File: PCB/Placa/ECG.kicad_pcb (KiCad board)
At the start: 2 copper layers, 118.6 x 62.2 mm, 44 parts, among them P1 USB_OTG, P2 CONN_01X03, P3 CONN_01X03, P7 Shield, U1 INA333, U2 OPA2335, U3 OPA2335, U4 REF5050, U5 REF3112, U6 INA333, U7 OPA2335, U8 OPA2335

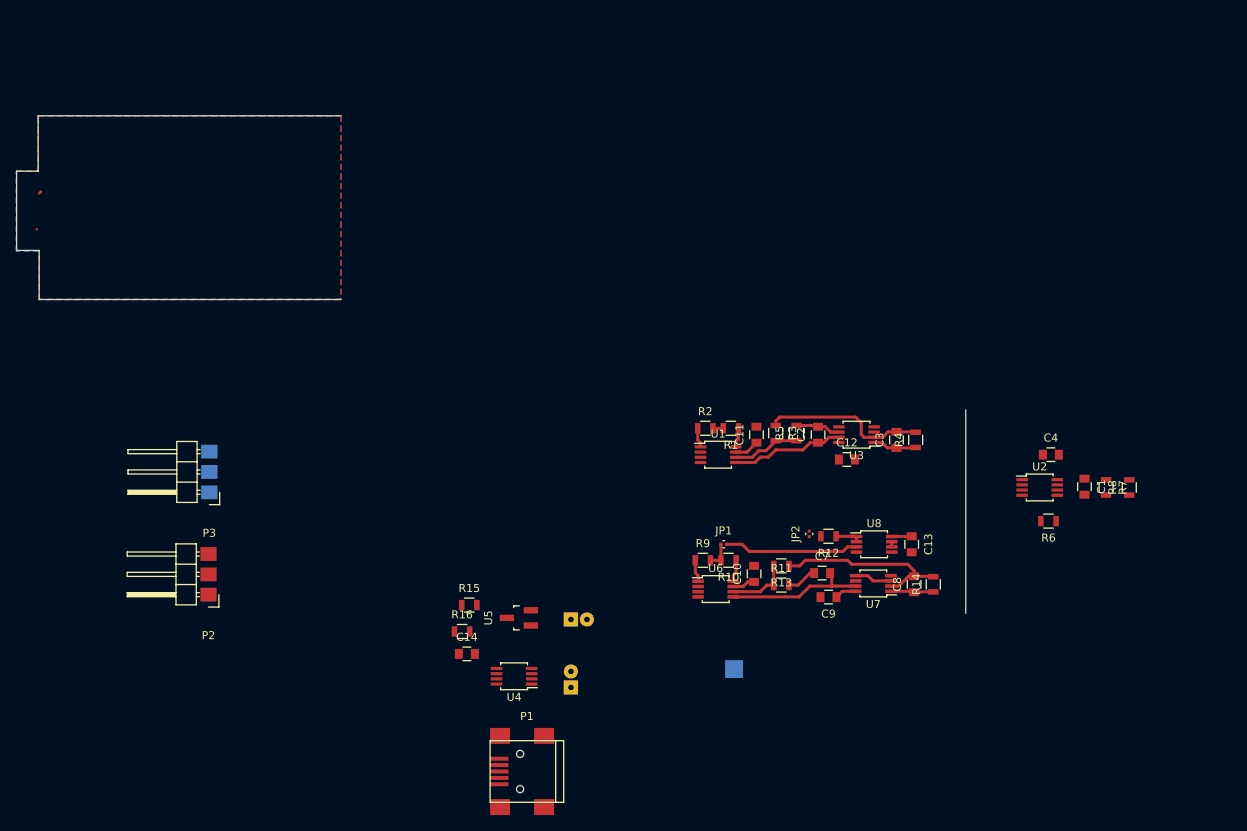
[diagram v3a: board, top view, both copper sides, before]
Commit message: Sigo con la placa. Agregué el micrófono electret
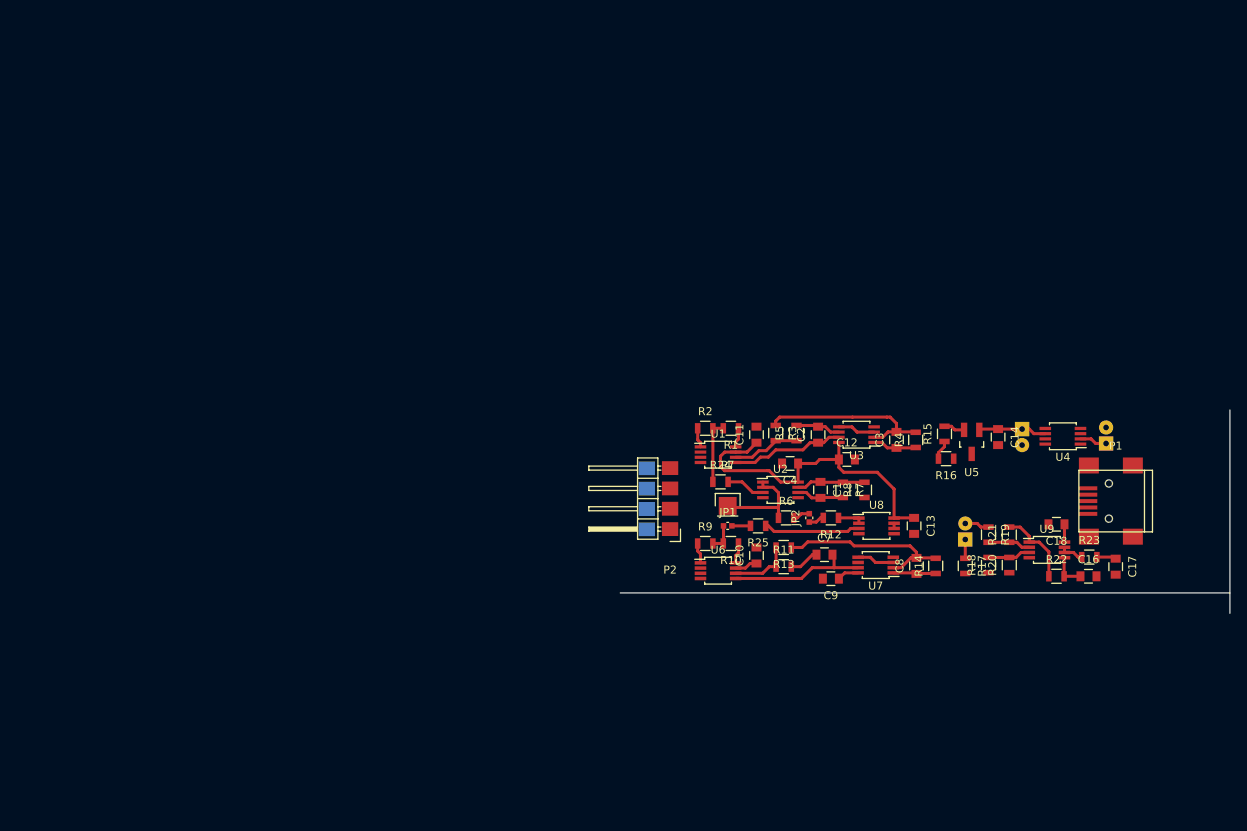
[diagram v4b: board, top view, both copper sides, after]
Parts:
- added C15: 4.7u, Capacitors_ThroughHole:C_Radial_D5_L11_P2, B.Cu at (175.2, 87.3)
- added C16: 470n, Capacitors_SMD:C_0805, F.Cu at (190.6, 91.9)
- added C17: 470n, Capacitors_SMD:C_0805, F.Cu at (194.0, 90.7)
- added C18: 0.1u, Capacitors_SMD:C_0805, F.Cu at (186.6, 85.4)
- added R17: 2.2k, Resistors_SMD:R_0805, F.Cu at (175.2, 90.6)
- added R18: 1.1k, Resistors_SMD:R_0805, F.Cu at (178.1, 90.5)
- added R19: 10k, Resistors_SMD:R_0805, F.Cu at (178.1, 86.7)
- added R20: 2.2k, Resistors_SMD:R_0805, F.Cu at (180.7, 90.5)
- added R21: 100k, Resistors_SMD:R_0805, F.Cu at (180.7, 86.7)
- added R22: 3.3k, Resistors_SMD:R_0805, F.Cu at (186.6, 91.9)
- added R23: 3.3k, Resistors_SMD:R_0805, F.Cu at (190.7, 89.5)
- added R24: 100k, Resistors_SMD:R_0805, F.Cu at (144.6, 80.1)
- added R25: 100k, Resistors_SMD:R_0805, F.Cu at (149.3, 85.6)
- added U9: OPA2335, Housings_SSOP:MSOP-8_3x3mm_Pitch0.65mm, F.Cu at (185.4, 88.6)
- P2: value CONN_01X03 -> CONN_01X04; footprint Pin_Headers:Pin_Header_Angled_1x03 -> Pin_Headers:Pin_Header_Angled_1x04
- P3: value CONN_01X03 -> CONN_01X04; footprint Pin_Headers:Pin_Header_Angled_1x03 -> Pin_Headers:Pin_Header_Angled_1x04; moved to B.Cu
- P7: moved to F.Cu
- moved P1 81.0 mm to (194.0, 82.5)
- moved U4 74.9 mm to (187.4, 74.4)
- moved C5 73.5 mm to (192.8, 75.3)
- moved C14 71.7 mm to (179.3, 74.5), turned to 270 degrees
- moved R16 64.2 mm to (172.8, 77.2), turned to 180 degrees
- moved R15 63.1 mm to (172.6, 74.1), turned to 90 degrees
- moved C6 61.2 mm to (182.3, 73.5), turned to 270 degrees
- moved U5 60.7 mm to (176.0, 75.1), turned to 180 degrees
- moved P2 58.3 mm to (138.3, 86.0)
- moved P3 54.8 mm to (135.4, 78.4)
- moved R8 33.1 mm to (162.6, 81.1)
- moved C1 33.0 mm to (157.1, 81.1)
- moved R7 32.9 mm to (159.9, 81.1)
- moved R6 32.8 mm to (152.8, 84.6), turned to 0 degrees
- moved C4 32.6 mm to (153.3, 77.8), turned to 180 degrees
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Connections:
- P1 pad 4: (no net) -> /OUT_Mic
- P2 pad 1: /RA_ch1 -> /RA_ch2
- P2 pad 2: /RA_ch2 -> /LL_ch2
- P2 pad 3: /RL -> /RA_ch1
- P3 pad 1: /LL_ch1 -> /Mic
- P3 pad 2: /LL_ch2 -> (no net)
- P3 pad 3: (no net) -> /RL
- U2 pad 3: Net-(R1-Pad2) -> Net-(R24-Pad2)
- U8 pad 3: Net-(JP1-Pad2) -> Net-(R25-Pad1)
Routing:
- net +5V: track 11.1 -> 58.2 mm
- net Net-(JP1-Pad2): track 16.9 -> 2.33 mm
- net /SHIELD: track 0.00 -> 12.5 mm
- net Net-(R25-Pad1): track 0.00 -> 12.1 mm
- net Net-(R21-Pad2): track 0.00 -> 9.71 mm
- net Net-(C1-Pad1): track 0.00 -> 8.60 mm
- net /filtro: track 0.00 -> 8.07 mm
- net /REF: track 4.67 -> 11.9 mm
- net Net-(R1-Pad2): track 1.30 -> 8.00 mm
- net Net-(R19-Pad2): track 0.00 -> 5.36 mm
- net Net-(R18-Pad2): track 0.00 -> 5.36 mm
- net Net-(R24-Pad2): track 0.00 -> 4.90 mm
- net Net-(C16-Pad1): track 0.00 -> 4.40 mm
- net +BATT: track 0.00 -> 3.44 mm
- net Net-(C15-Pad2): track 0.00 -> 3.09 mm
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- removed copper zone on F.Cu, net +5V
- removed copper zone on B.Cu, net GND
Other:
- board size 118.6 x 62.2 mm -> 76.2 x 25.4 mm

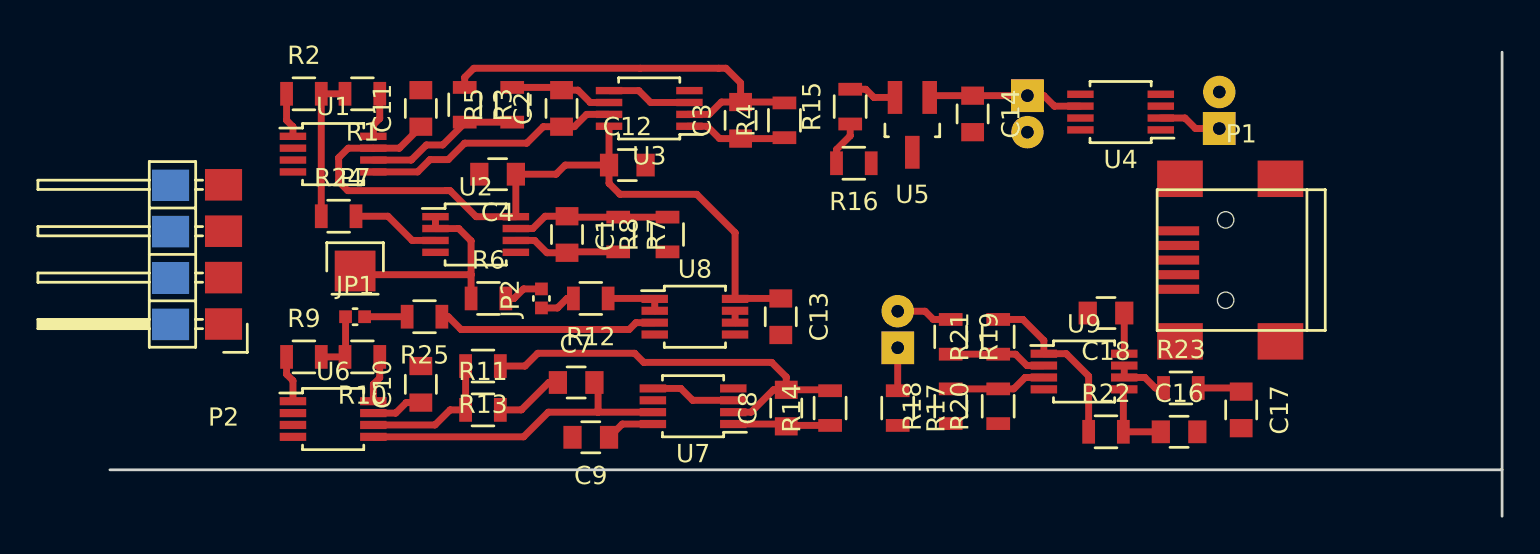
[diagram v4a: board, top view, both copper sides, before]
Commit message: Sigo con la placa. Vamos a poner un conector DIN
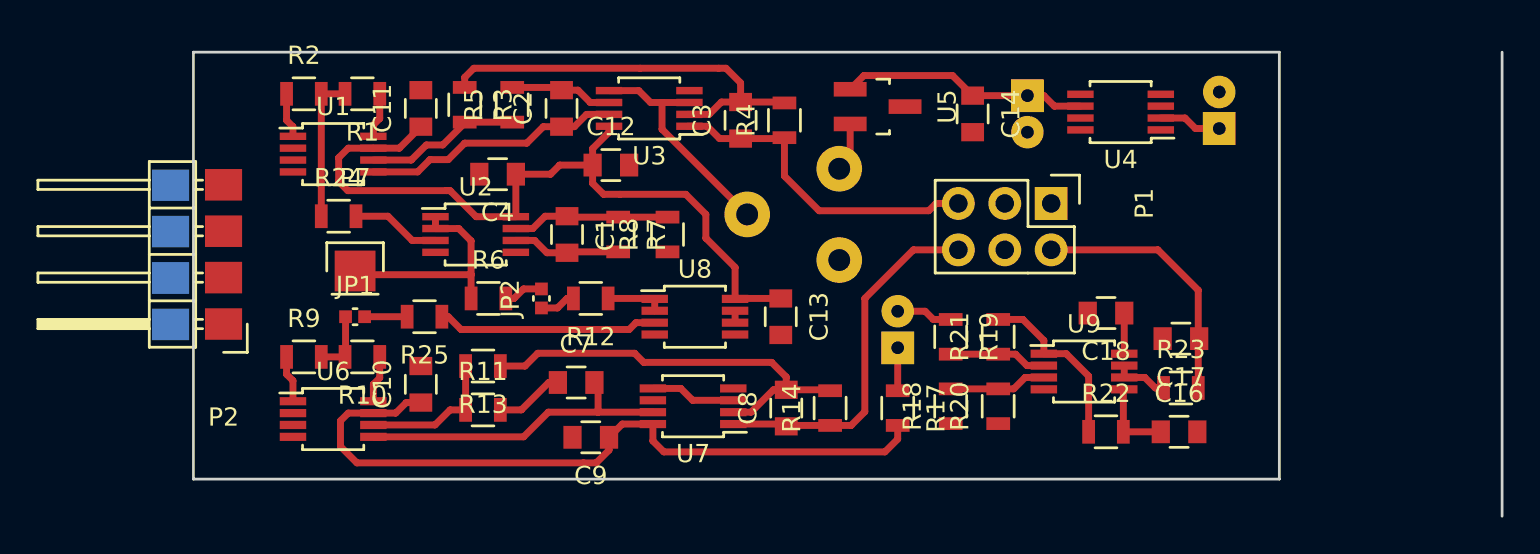
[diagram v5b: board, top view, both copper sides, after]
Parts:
- removed R15, R16: 4.7k, Resistors_SMD:R_0805
- added RV1: 10k, Potentiometers:Potentiometer_Triwood_RM-065, B.Cu at (172.0, 77.5)
- P1: value USB_OTG -> CONECTOR_DIN; footprint Connect:USB_Mini-B -> Pin_Headers:Pin_Header_Straight_2x03
- moved P1 10.9 mm to (183.6, 79.4), turned to 270 degrees
- moved C17 5.11 mm to (190.7, 86.8), turned to 180 degrees
- moved U5 2.15 mm to (174.1, 74.1), turned to 270 degrees
- moved C12 0.90 mm to (159.5, 77.3)
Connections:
- P1 pad 2: /OUT_ch2 -> /OUT_Mic
- P1 pad 3: /OUT_ch1 -> /SHIELD
- P1 pad 4: /OUT_Mic -> GND
- P1 pad 5: GND -> /OUT_ch1
- P1 pad 6: /SHIELD -> /OUT_ch2
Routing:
- net +5V: track 58.2 -> 98.4 mm
- net /OUT_ch2: track 5.37 -> 20.0 mm
- net /OUT_ch1: track 5.60 -> 18.2 mm
- net /OUT_Mic: track 2.43 -> 14.3 mm
- net /REF: track 11.9 -> 17.5 mm
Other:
- board size 76.2 x 25.4 mm -> 71.6 x 25.4 mm

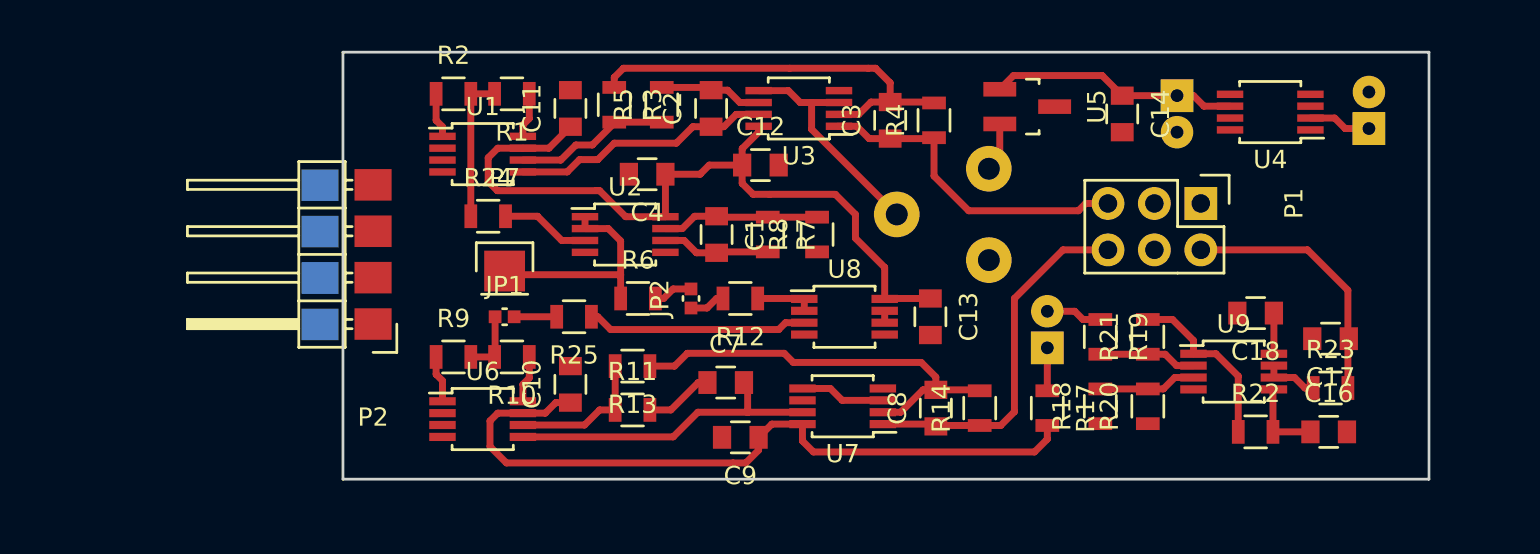
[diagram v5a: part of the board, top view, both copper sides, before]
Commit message: Pongo REF en VCC/2 y borro la referencia de 1,25V. Separo los canales y el micrófono en hojas distintas. Empiezo a modificar la placa
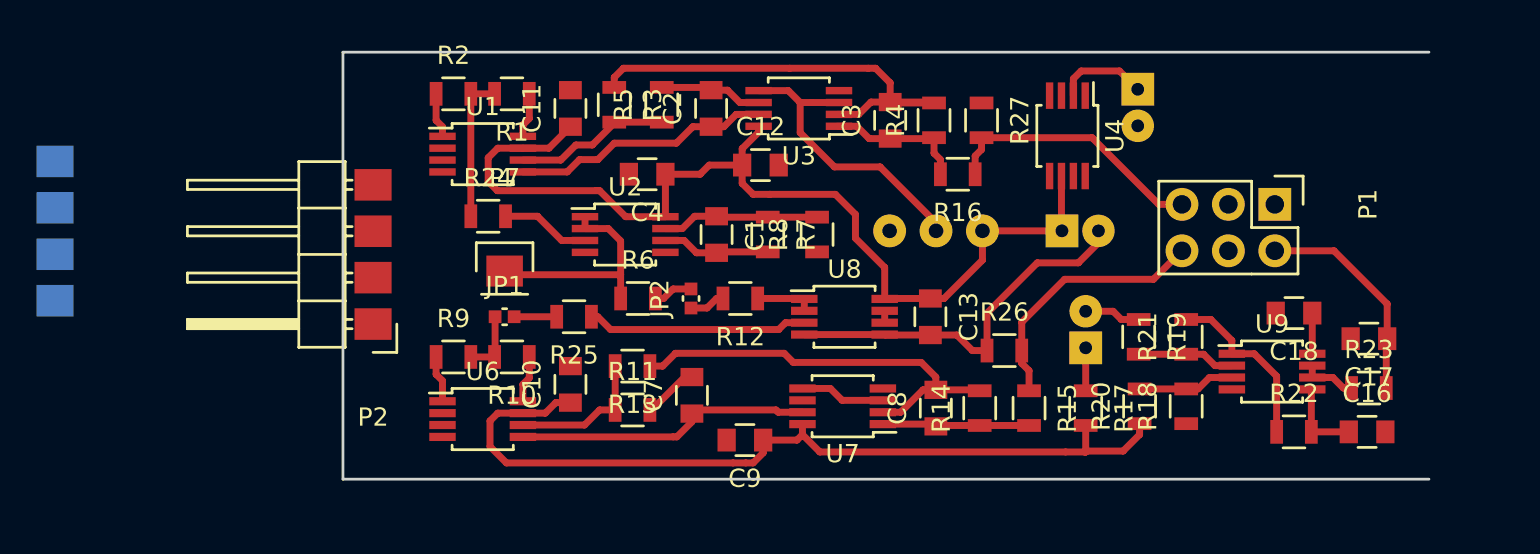
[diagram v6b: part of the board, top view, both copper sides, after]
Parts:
- removed C14: 0.47u, Capacitors_SMD:C_0805
- removed U5: REF3112, TO_SOT_Packages_SMD:SOT-23_Handsoldering
- added R15: 4,7k, Resistors_SMD:R_0805, F.Cu at (174.2, 90.6)
- added R16: 4,7k, Resistors_SMD:R_0805, F.Cu at (170.3, 77.8)
- added R26: 9,1k, Resistors_SMD:R_0805, F.Cu at (172.8, 87.5)
- added R27: 9,1k, Resistors_SMD:R_0805, F.Cu at (171.6, 74.8)
- P1: value CONECTOR_DIN -> A_CONECTOR_DIN
- RV1: footprint Potentiometers:Potentiometer_Triwood_RM-065 -> Potentiometers:Potentiometer_Bourns_3296W_3-8Zoll_Inline_ScrewUp
- moved P3 14.6 mm to (120.9, 77.1)
- moved C5 12.8 mm to (180.2, 73.2), turned to 270 degrees
- moved U4 11.2 mm to (176.3, 75.7), turned to 270 degrees
- moved C6 9.72 mm to (176.0, 80.9), turned to 0 degrees
- moved R18 4.70 mm to (182.8, 90.5)
- moved P1 4.05 mm to (187.7, 79.5)
- moved RV1 3.42 mm to (171.7, 80.9)
- moved C15 2.10 mm to (177.3, 87.3)
- moved C17 2.10 mm to (192.8, 86.8)
- moved R17 2.10 mm to (177.3, 90.6)
- moved R21 2.10 mm to (182.8, 86.7)
- moved R23 2.10 mm to (192.8, 89.5)
- moved C16 2.10 mm to (192.7, 91.9)
- moved C18 2.10 mm to (188.7, 85.4)
- moved R19 2.10 mm to (180.2, 86.7)
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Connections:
- net /LL_ch1 renamed /Canales_ECG/LA_ch1
- net /LL_ch2 renamed /Canales_ECG/LA_ch2
- net /Mic renamed /Microfono/Mic
- net /OUT_Mic renamed /Microfono/OUT_Mic
- net /RA_ch1 renamed /Canales_ECG/RA_ch1
- net /RA_ch2 renamed /Canales_ECG/RA_ch2
- net /REF renamed /Canales_ECG/REF
- net /RL renamed /Canales_ECG/RL
- net /SHIELD renamed /Canales_ECG/SHIELD
- net /filtro renamed /Canales_ECG/filtro
- C3 pad 1: /OUT_ch1 -> Net-(C3-Pad1)
- C8 pad 1: /OUT_ch2 -> Net-(C8-Pad1)
- P1 pad 5: /OUT_ch1 -> /Canales_ECG/OUT_ch1
- P1 pad 6: /OUT_ch2 -> /Canales_ECG/OUT_ch2
- R14 pad 1: /OUT_ch2 -> Net-(C8-Pad1)
- R4 pad 1: /OUT_ch1 -> Net-(C3-Pad1)
- RV1 pad 1: Net-(RV1-Pad1) -> +5V
- U3 pad 1: /OUT_ch1 -> Net-(C3-Pad1)
- U7 pad 1: /OUT_ch2 -> Net-(C8-Pad1)
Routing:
- net GND: track 0.11 -> 20.9 mm
- net /OUT_ch2: track 20.0 -> 0.00 mm
- net /OUT_ch1: track 18.2 -> 0.00 mm
- net /Canales_ECG/OUT_ch1: track 0.00 -> 16.1 mm
- net /Canales_ECG/OUT_ch2: track 0.00 -> 16.0 mm
- net Net-(C3-Pad1): track 0.00 -> 9.11 mm
- net Net-(C8-Pad1): track 0.00 -> 8.07 mm
- net +5V: track 98.4 -> 103.5 mm
- net /Canales_ECG/REF: track 17.5 -> 20.9 mm
- net Net-(RV1-Pad1): track 2.70 -> 0.00 mm
- net Net-(C7-Pad1): track 19.1 -> 16.6 mm
- net Net-(C3-Pad2): track 23.2 -> 25.6 mm
- net /Microfono/OUT_Mic: track 14.3 -> 11.9 mm
- net +BATT: track 3.44 -> 5.04 mm
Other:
- board text added: "4mm desde el borde de la placa hasta el final del pin"

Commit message: Sigo ruteando
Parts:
- moved P3 17.5 mm to (138.3, 79.0)
- moved P7 3.60 mm to (142.5, 85.1)
- moved R24 1.87 mm to (144.6, 82.0)
- moved R7 1.19 mm to (159.7, 79.9)
- moved C1 1.16 mm to (157.0, 79.9)
- moved C13 0.76 mm to (168.8, 84.8)
- moved C7 0.70 mm to (155.1, 89.9)
- moved P2 0.61 mm to (138.3, 86.6)
- moved JP1 0.57 mm to (144.9, 85.5), turned to 90 degrees
- moved C8 0.55 mm to (168.9, 91.1)
- moved R13 0.53 mm to (152.0, 88.3)
- moved R11 0.53 mm to (152.0, 90.7)
- moved R14 0.51 mm to (171.5, 91.1)
- moved R15 0.51 mm to (174.2, 91.1)
- moved C12 0.50 mm to (159.0, 77.1)
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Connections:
- P3 pad 1: /Microfono/Mic -> GND
- P3 pad 2: (no net) -> /Canales_ECG/RL
- P3 pad 3: /Canales_ECG/RL -> (no net)
- P3 pad 4: GND -> /Microfono/Mic
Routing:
- net GND: track 20.9 -> 122.2 mm, vias 0 -> 5
- net /Microfono/Mic: track 2.35 -> 46.8 mm
- net +5V: track 103.5 -> 135.1 mm
- net /Canales_ECG/REF: track 20.9 -> 50.1 mm, vias 0 -> 2
- net /Canales_ECG/RL: track 0.00 -> 25.5 mm, vias 0 -> 1
- net /Canales_ECG/OUT_ch2: track 16.0 -> 2.47 mm
- net /Canales_ECG/OUT_ch1: track 16.1 -> 4.16 mm
- net /Canales_ECG/LA_ch2: track 0.00 -> 9.52 mm
- net /Canales_ECG/RA_ch1: track 0.00 -> 7.66 mm
- net Net-(C7-Pad2): track 3.05 -> 10.7 mm
- net /Canales_ECG/RA_ch2: track 0.00 -> 7.47 mm
- net /Canales_ECG/LA_ch1: track 0.00 -> 5.70 mm
- net Net-(C8-Pad2): track 23.0 -> 27.7 mm
- net /Canales_ECG/SHIELD: track 12.5 -> 16.7 mm
- net Net-(R11-Pad1): track 7.79 -> 4.86 mm
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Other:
- board size 71.6 x 25.4 mm -> 59.9 x 25.4 mm
